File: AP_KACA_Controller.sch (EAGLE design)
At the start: 44 parts, among them IC2 REG710XX-3.3, J1 FTDI_DEVICE, M1 WIRELESS-NRF24L01, Y1 8MHz

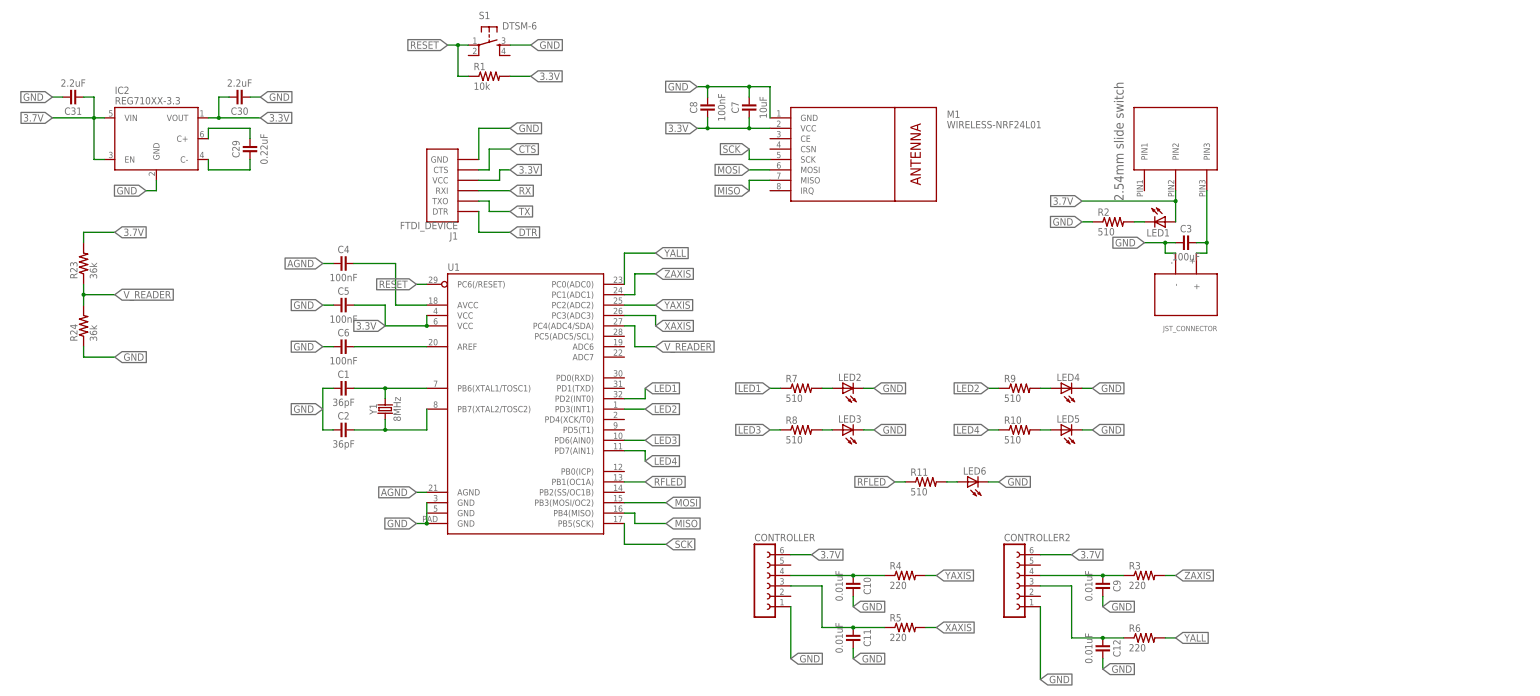
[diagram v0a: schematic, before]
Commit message: added missing components
there were some missing labels and parts of the schematic
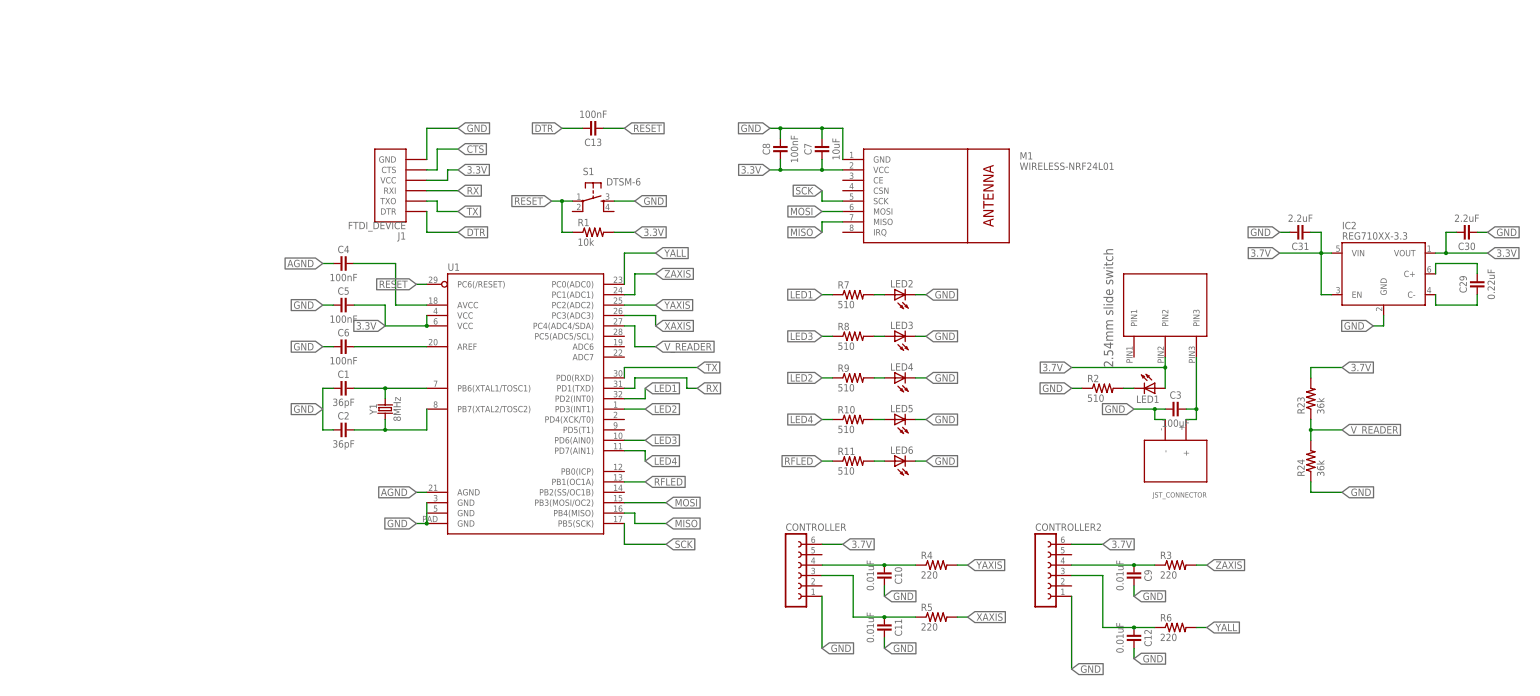
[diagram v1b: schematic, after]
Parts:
- added C13: 100nF, we-rcl:CAPACITOR-0603
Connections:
- net DTR: now also C13.2
- net RESET: now also C13.1
- net RX: now also U1.PD1(TXD)
- net TX: now also U1.PD0(RXD)
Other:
- moved on the sheet: C10, C11, C12, C29, C3, C30, C31, C7, C8, C9, CONTROLLER, CONTROLLER2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
